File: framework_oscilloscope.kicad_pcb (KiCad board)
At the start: 4 copper layers, 26 x 44 mm, 79 parts, among them IC1 FT232HL-REEL, IC10 93LC56BT-I_OT, IC2 ICE40UP5K-SG48I, IC3 ADC08060CIMTX_NOPB, IC7 OPA356AIDBVR, IC8 TLV77312PDBVR, IC9 LM4040C20IDBZT, J1 BNC, P1 USB_C_Plug_USB2.0, U9 TPS62A02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

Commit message: cleanup, and a little routing
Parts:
- moved C26 85.2 mm to (63.0, 82.5), turned to 180 degrees
- moved C10 84.1 mm to (76.1, 100.3)
- moved C12 84.1 mm to (66.1, 99.8)
- moved C19 84.1 mm to (66.1, 94.8)
- moved C21 84.1 mm to (65.1, 94.8)
- moved C29 84.1 mm to (72.6, 82.8)
- moved C33 84.1 mm to (65.1, 86.8)
- moved C36 84.1 mm to (75.1, 82.2)
- moved C37 84.1 mm to (63.1, 90.6)
- moved C40 84.1 mm to (76.8, 117.2)
- moved C7 84.1 mm to (59.9, 102.2)
- moved IC1 84.1 mm to (71.1, 88.5)
- moved R8 84.1 mm to (63.5, 99.5)
- moved C11 84.1 mm to (64.9, 100.4)
- moved C13 84.1 mm to (64.9, 97.4)
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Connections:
- C27 pad 1: Net-(Y1-TRI-STATE) -> +3V3
- C5 pad 1: +VUSB -> VBUS
- C6 pad 1: +VUSB -> VBUS
- R7 pad 1: +VUSB -> VBUS
- U9 pad 3: +VUSB -> VBUS
- Y1 pad 1: Net-(Y1-TRI-STATE) -> +3V3
- Y1 pad 4: Net-(Y1-TRI-STATE) -> +3V3
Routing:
- net VBUS: track 0.00 -> 61.7 mm, vias 0 -> 6
- net /USB_DP: track 0.00 -> 25.6 mm
- net /USB_DN: track 0.00 -> 25.1 mm
- net +3V3: track 3.01 -> 14.7 mm
- net GND: track 7.78 -> 14.8 mm, vias 35 -> 49
- net Net-(P1-CC): track 0.00 -> 6.79 mm
- net /SPI_SO: track 1.04 -> 7.75 mm, vias 1 -> 2
- net /SPI_SCK: track 1.24 -> 6.60 mm, vias 1 -> 2
- net +1V2: track 15.5 -> 11.5 mm, vias 4 -> 3
- net Net-(U9-FB): track 0.00 -> 2.77 mm
- net Net-(IC1A-REF): track 1.29 -> 3.49 mm
- net Net-(U9-SW): track 0.00 -> 2.12 mm
- net Net-(IC1A-~{RESET}): track 0.00 -> 1.89 mm
- added copper zone on B.Cu, net GND
- added copper zone on B.Cu, net VBUS
- added copper zone on F.Cu, net VBUS
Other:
- board text added: "STACKUP: JLC04161H_3313"

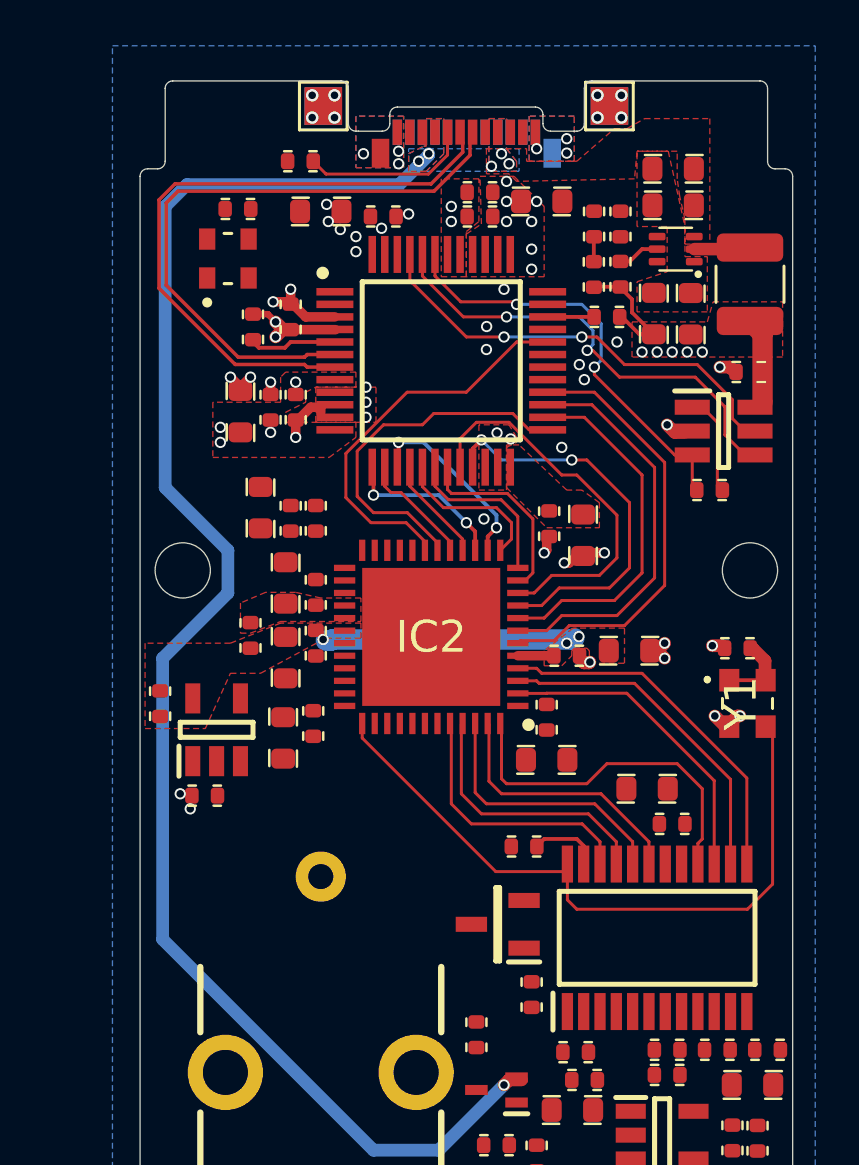
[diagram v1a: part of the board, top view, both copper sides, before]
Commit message: small sch tweek, almost done routing
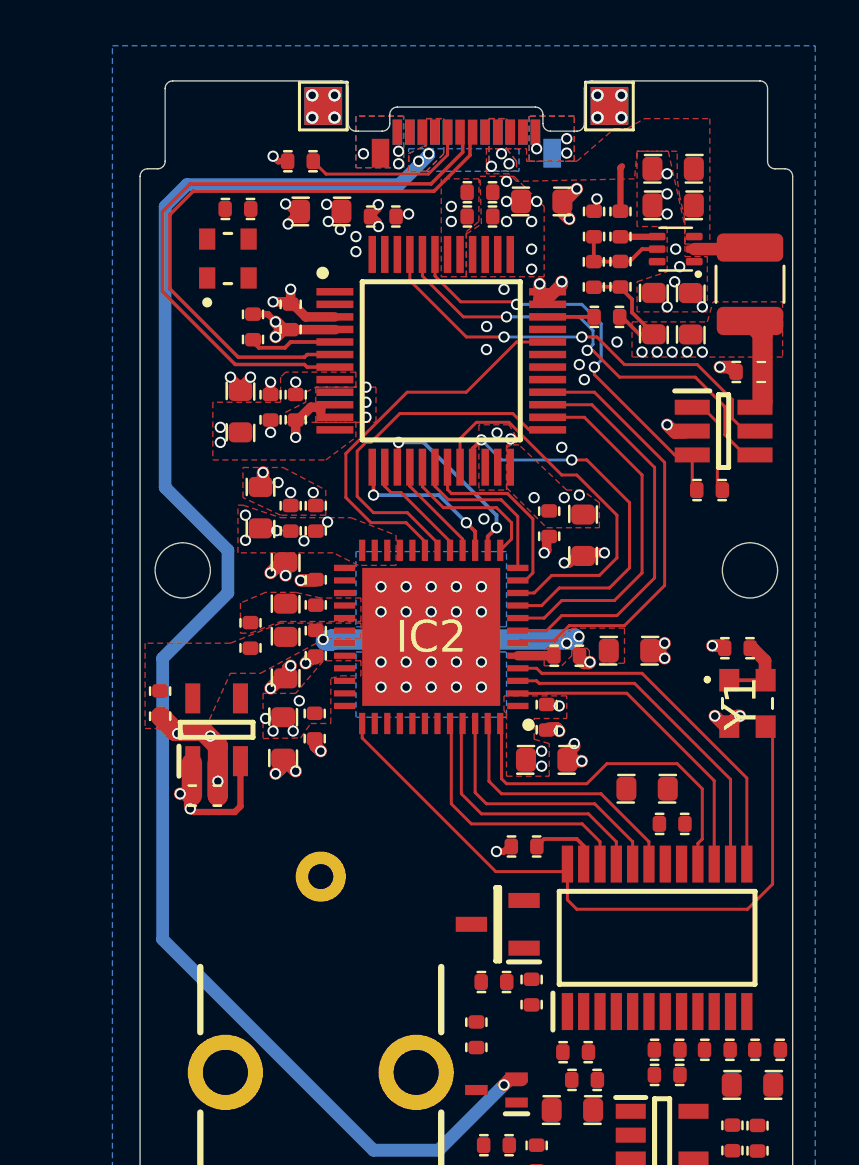
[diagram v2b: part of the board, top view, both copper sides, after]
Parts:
- added C47: 100nF, framework_oscilloscope:0402_1005Metric_CAP, F.Cu at (73.2, 113.3)
- C25: value 1uF -> 100nF
- moved C17 0.12 mm to (66.1, 103.1)
- moved R13 0.10 mm to (74.7, 113.7), turned to -90 degrees
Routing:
- net GND: track 14.8 -> 34.6 mm, vias 49 -> 106
- net +3V3: track 14.7 -> 20.7 mm, vias 24 -> 39
- net VBUS: track 61.7 -> 63.5 mm
- net Net-(U9-EN): track 0.00 -> 1.46 mm
- net Net-(U9-FB): track 2.77 -> 3.79 mm

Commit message: done routing
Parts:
- moved C39 0.20 mm to (80.1, 107.0)
- moved R11 0.16 mm to (74.9, 120.2)
- moved C44 0.11 mm to (84.0, 116.0)
- moved C26 0.11 mm to (62.9, 82.5), turned to 0 degrees
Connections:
- C26 pad 2: Net-(Y2-GND) -> GND
- Y2 pad 2: Net-(Y2-GND) -> GND
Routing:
- net VBUS: track 63.5 -> 81.1 mm, vias 6 -> 8
- net GND: track 34.6 -> 49.2 mm, vias 106 -> 141
- net +3V3: track 20.7 -> 30.3 mm, vias 39 -> 56
- net Net-(J1-Signal): track 0.00 -> 8.62 mm
- net Net-(IC7--IN): track 0.00 -> 5.94 mm
- net Net-(IC7-+IN): track 0.00 -> 5.20 mm
- net +2V048: track 0.00 -> 5.16 mm, vias 0 -> 4
- net Net-(IC1A-XCSI): track 0.00 -> 4.32 mm
- net Net-(D1-K/A): track 0.00 -> 3.92 mm
- net /ADC_VIN: track 0.00 -> 2.57 mm
- net Net-(IC3B-VRM): track 0.00 -> 1.57 mm
- added copper zone on F.Cu, net +2V048

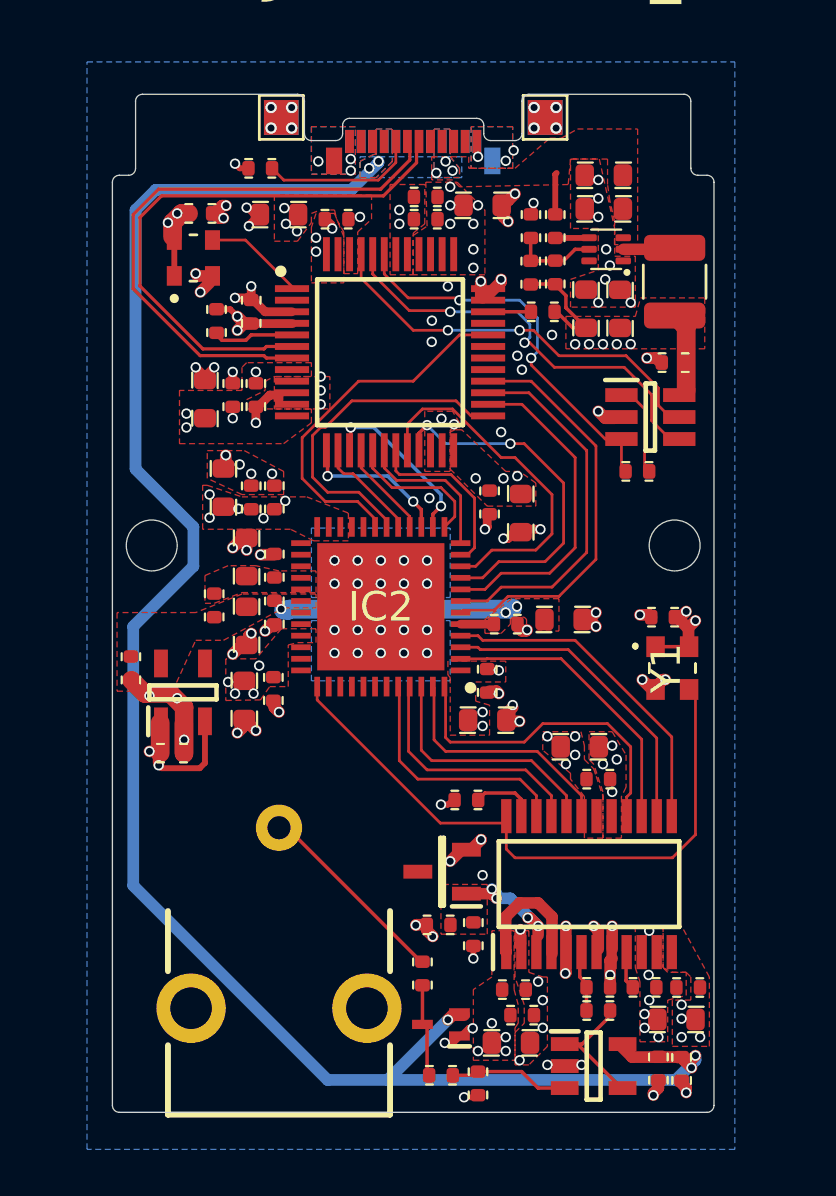
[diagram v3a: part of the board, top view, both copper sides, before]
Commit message: fixed emc errors, fixed drc errors
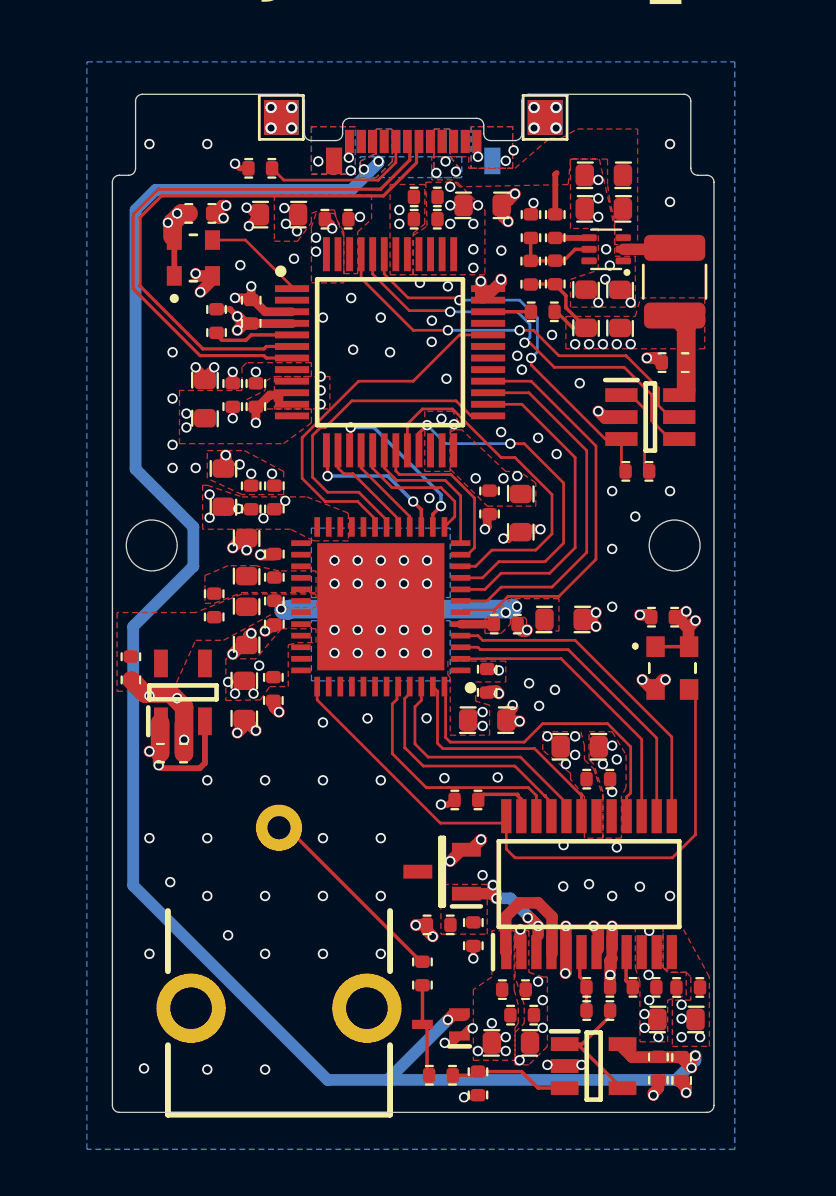
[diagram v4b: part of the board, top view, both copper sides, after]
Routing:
- net GND: vias 141 -> 204

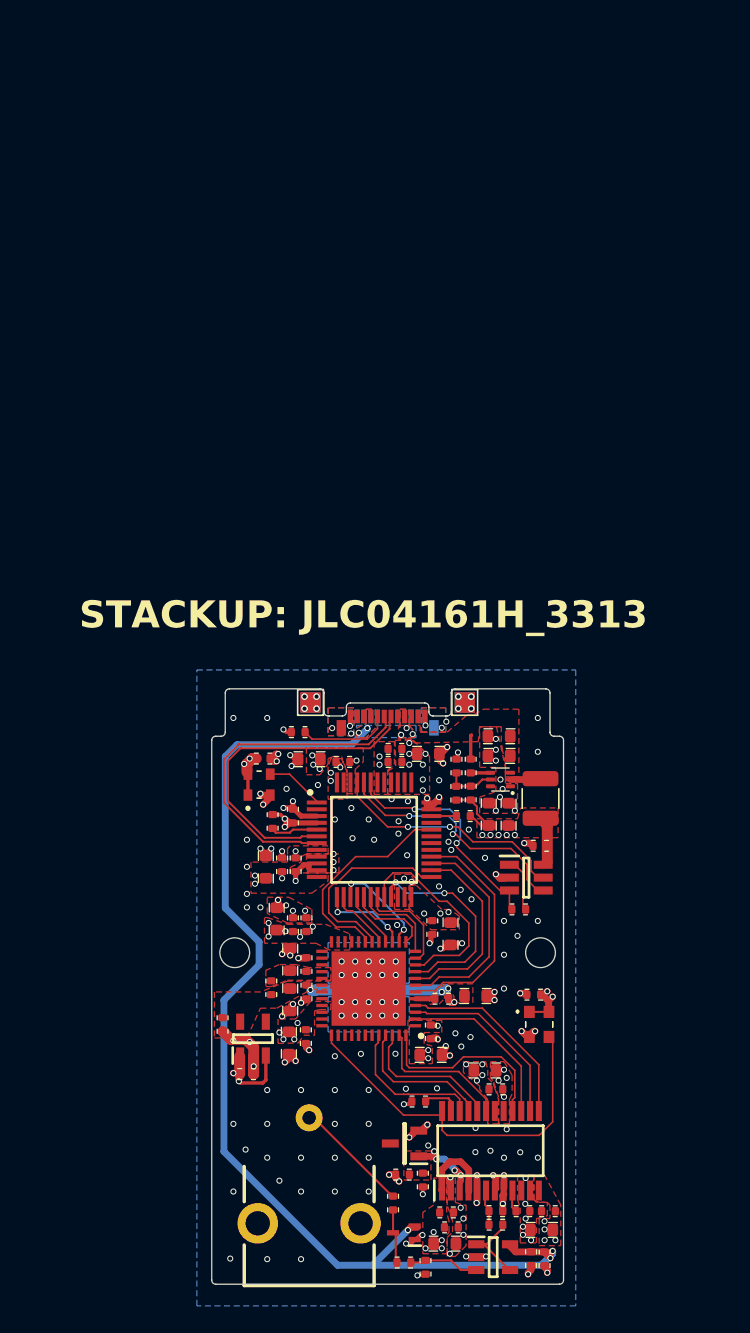
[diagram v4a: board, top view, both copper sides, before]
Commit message: changed layout frame size
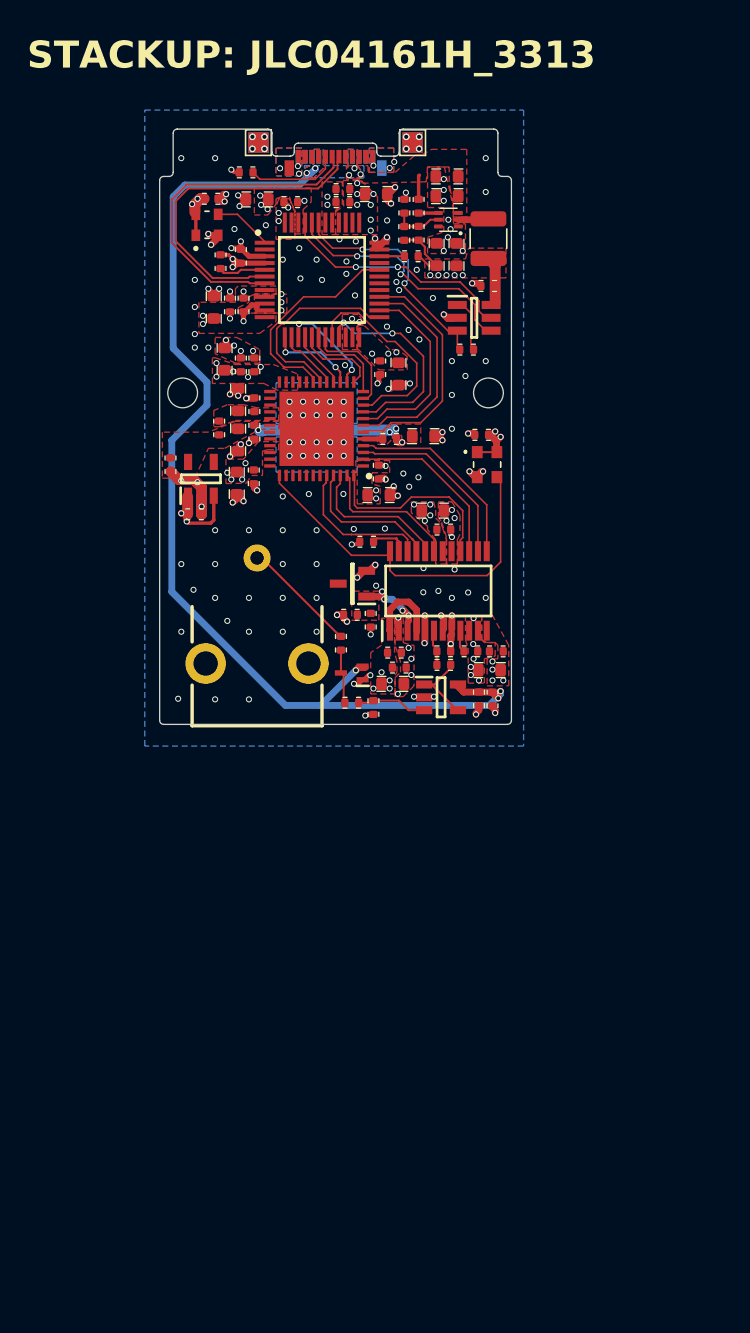
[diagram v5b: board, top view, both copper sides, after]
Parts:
- moved C13 41.6 mm to (61.0, 56.0)
- moved C14 41.6 mm to (62.2, 56.4)
- moved C17 41.6 mm to (62.2, 61.7)
- moved C20 41.6 mm to (60.0, 53.0)
- moved C30 41.6 mm to (60.5, 49.0)
- moved C32 41.6 mm to (61.5, 49.0)
- moved C34 41.6 mm to (71.5, 53.7)
- moved C46 41.6 mm to (79.5, 47.6)
- moved C5 41.6 mm to (76.5, 39.5)
- moved C6 41.6 mm to (76.5, 41.0)
- moved H1 41.6 mm to (57.0, 55.5)
- moved H2 41.6 mm to (79.5, 55.5)
- moved P1 41.6 mm to (68.2, 38.0)
- moved R5 41.6 mm to (73.3, 43.7)
- moved R6 41.6 mm to (73.3, 41.7)
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
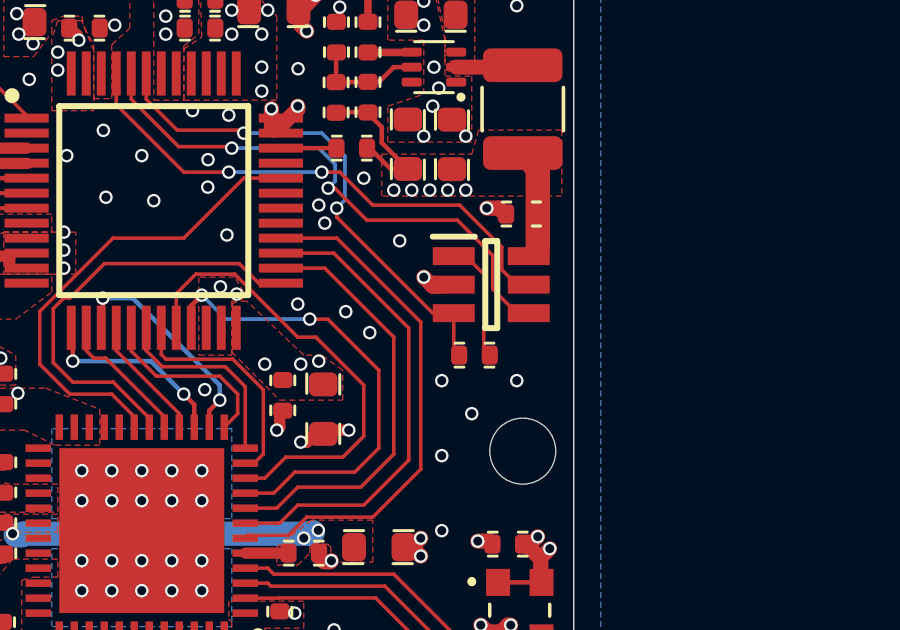
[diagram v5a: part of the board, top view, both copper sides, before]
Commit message: added pull ups to eeprom->ftdi spi, as per reference design (tri state pins on FT232 SPI)
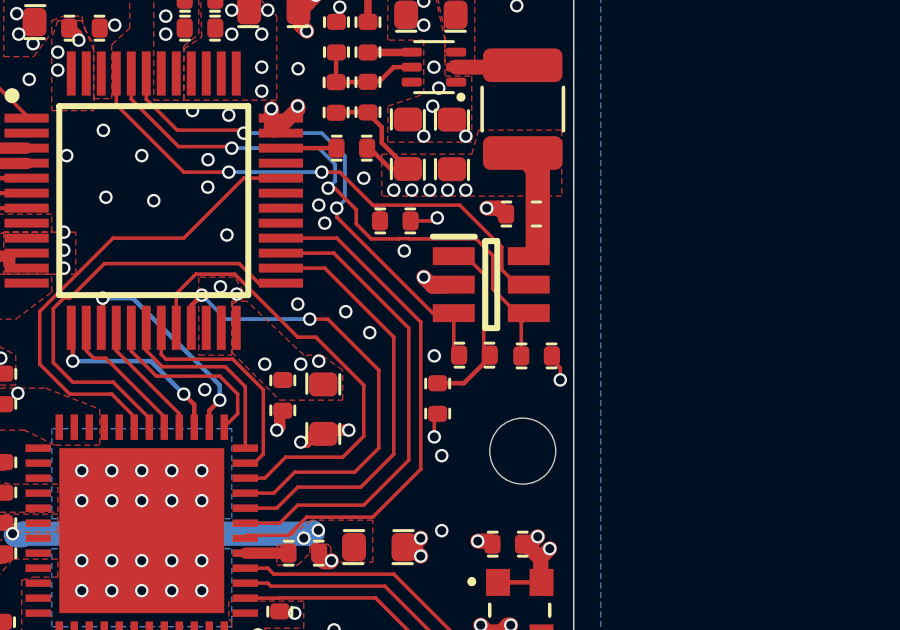
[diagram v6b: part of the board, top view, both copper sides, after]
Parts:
- added R15: 10kR, framework_oscilloscope:0402_1005Metric, F.Cu at (76.7, 53.8)
- added R16: 10kR, framework_oscilloscope:0402_1005Metric, F.Cu at (80.0, 52.4)
- added R17: 10kR, framework_oscilloscope:0402_1005Metric, F.Cu at (75.3, 47.9)
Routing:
- net +3V3: track 30.3 -> 32.8 mm, vias 56 -> 59
- net Net-(IC10-DO): track 4.03 -> 6.20 mm
- net Net-(IC10-CLK): track 18.5 -> 20.3 mm
- net Net-(IC10-CS): track 17.7 -> 18.3 mm
- net GND: vias 204 -> 202
